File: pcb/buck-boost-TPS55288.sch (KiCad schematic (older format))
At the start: 20 parts

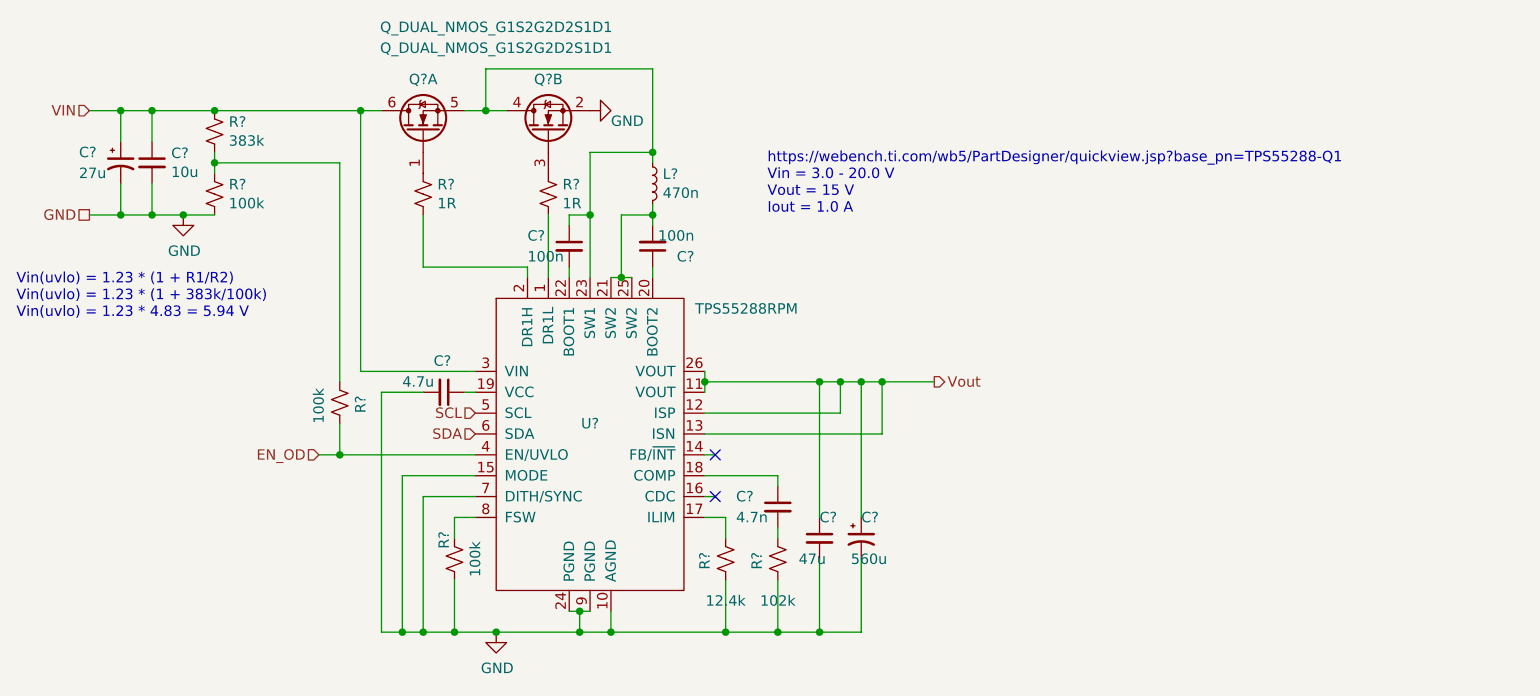
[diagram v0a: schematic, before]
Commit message: [PCB] update mcu config & pwr converter, add sd card
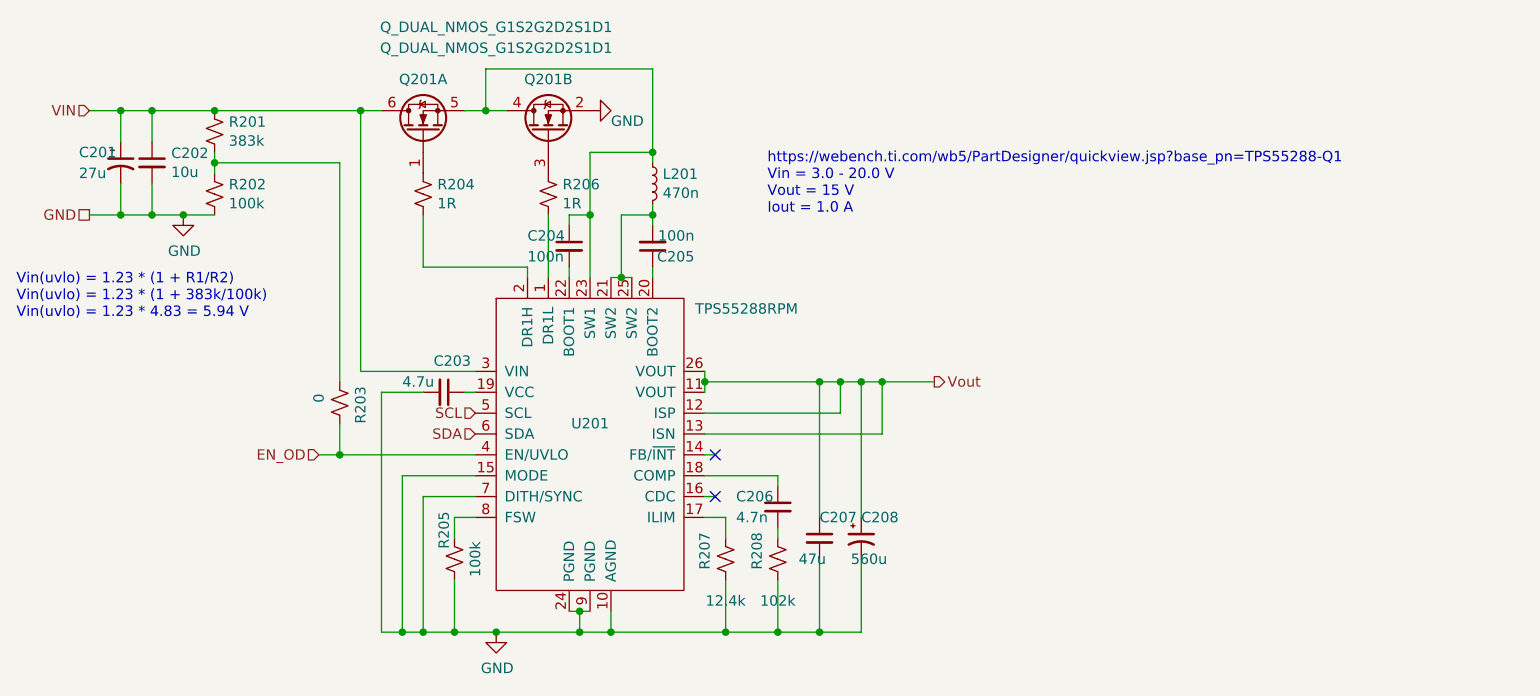
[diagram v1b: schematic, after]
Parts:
- R203: renamed from R?; value 100k -> 0
- gave numbers to parts that had none: 18
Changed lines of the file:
@@
 $Descr A4 11693 8268
 encoding utf-8
-Sheet 2 4
+Sheet 2 5
 Title ""
 Date ""
@@
 $EndDescr
 $Comp
-L project-lib:TPS55288RPM U?
+L project-lib:TPS55288RPM U201
 U 1 1 605DA098
 P 5850 3750
-F 0 "U?" H 5850 3850 50  0000 C CNN
+F 0 "U201" H 5850 3850 50  0000 C CNN
 F 1 "TPS55288RPM" H 6600 4400 50  0000 C CNN
 F 2 "" H 5850 3600 50  0001 C CNN
@@
 GND
 $Comp
-L Device:CP1_Small C?
+L Device:CP1_Small C201
 U 1 1 605DAB16
 P 3600 2400
-F 0 "C?" H 3400 2450 50  0000 L CNN
+F 0 "C201" H 3400 2450 50  0000 L CNN
 F 1 "27u" H 3400 2350 50  0000 L CNN
 F 2 "" H 3600 2400 50  0001 C CNN
@@
 $EndComp
 $Comp
-L Device:R_Small_US R?
+L Device:R_Small_US R201
 U 1 1 605DCCBF
 P 4050 2250
-F 0 "R?" H 4118 2296 50  0000 L CNN
+F 0 "R201" H 4118 2296 50  0000 L CNN
 F 1 "383k" H 4118 2205 50  0000 L CNN
 F 2 "" H 4050 2250 50  0001 C CNN
@@
 $EndComp
 $Comp
-L Device:R_Small_US R?
+L Device:R_Small_US R202
 U 1 1 605DD936
 P 4050 2550
-F 0 "R?" H 4118 2596 50  0000 L CNN
+F 0 "R202" H 4118 2596 50  0000 L CNN
 F 1 "100k" H 4118 2505 50  0000 L CNN
 F 2 "" H 4050 2550 50  0001 C CNN
@@
 Connection ~ 4050 2150
 $Comp
-L Device:R_Small_US R?
+L Device:R_Small_US R204
 U 1 1 605E0D09
 P 5050 2550
-F 0 "R?" H 5118 2596 50  0000 L CNN
+F 0 "R204" H 5118 2596 50  0000 L CNN
 F 1 "1R" H 5118 2505 50  0000 L CNN
 F 2 "" H 5050 2550 50  0001 C CNN
@@
 $EndComp
 $Comp
-L power:GND #PWR?
+L power:GND #PWR0104
 U 1 1 605E1D02
 P 3900 2650
-F 0 "#PWR?" H 3900 2400 50  0001 C CNN
+F 0 "#PWR0104" H 3900 2400 50  0001 C CNN
 F 1 "GND" H 3905 2477 50  0000 C CNN
 F 2 "" H 3900 2650 50  0001 C CNN
@@
 	3900 2650 4050 2650
 $Comp
-L Device:Q_DUAL_NMOS_G1S2G2D2S1D1 Q?
+L Device:Q_DUAL_NMOS_G1S2G2D2S1D1 Q201
 U 1 1 605EB98C
 P 5050 2250
-F 0 "Q?" V 5300 2250 50  0000 C CNN
+F 0 "Q201" V 5300 2250 50  0000 C CNN
 F 1 "Q_DUAL_NMOS_G1S2G2D2S1D1" V 5550 1900 50  0000 C CNN
 F 2 "" H 5250 2250 50  0001 C CNN
@@
 $EndComp
 $Comp
-L Device:Q_DUAL_NMOS_G1S2G2D2S1D1 Q?
+L Device:Q_DUAL_NMOS_G1S2G2D2S1D1 Q201
 U 2 1 605ED468
 P 5650 2250
-F 0 "Q?" V 5900 2250 50  0000 C CNN
+F 0 "Q201" V 5900 2250 50  0000 C CNN
 F 1 "Q_DUAL_NMOS_G1S2G2D2S1D1" V 6050 2500 50  0000 C CNN
 F 2 "" H 5850 2250 50  0001 C CNN
@@
 	5550 2900 5550 2950
 $Comp
-L Device:R_Small_US R?
+L Device:R_Small_US R206
 U 1 1 605F4F86
 P 5650 2550
-F 0 "R?" H 5718 2596 50  0000 L CNN
+F 0 "R206" H 5718 2596 50  0000 L CNN
 F 1 "1R" H 5718 2505 50  0000 L CNN
 F 2 "" H 5650 2550 50  0001 C CNN
@@
 	5650 2650 5650 2950
 $Comp
-L power:GND #PWR?
+L power:GND #PWR0105
 U 1 1 605F59CE
 P 5850 2150
-F 0 "#PWR?" H 5850 1900 50  0001 C CNN
+F 0 "#PWR0105" H 5850 1900 50  0001 C CNN
 F 1 "GND" V 5800 2050 50  0000 R CNN
 F 2 "" H 5850 2150 50  0001 C CNN
@@
 $EndComp
 $Comp
-L Device:C_Small C?
+L Device:C_Small C202
 U 1 1 605F65FF
 P 3750 2400
-F 0 "C?" H 3842 2446 50  0000 L CNN
+F 0 "C202" H 3842 2446 50  0000 L CNN
 F 1 "10u" H 3842 2355 50  0000 L CNN
 F 2 "" H 3750 2400 50  0001 C CNN
@@
 $EndComp
 $Comp
-L Device:C_Small C?
+L Device:C_Small C204
 U 1 1 605F7034
 P 5750 2800
-F 0 "C?" H 5550 2850 50  0000 L CNN
+F 0 "C204" H 5550 2850 50  0000 L CNN
 F 1 "100n" H 5550 2750 50  0000 L CNN
 F 2 "" H 5750 2800 50  0001 C CNN
@@
 	5850 2650 5850 2950
 $Comp
-L Device:L_Small L?
+L Device:L_Small L201
 U 1 1 605FE001
 P 6150 2500
-F 0 "L?" H 6198 2546 50  0000 L CNN
+F 0 "L201" H 6198 2546 50  0000 L CNN
 F 1 "470n" H 6198 2455 50  0000 L CNN
 F 2 "" H 6150 2500 50  0001 C CNN
@@
 Connection ~ 5850 2650
 $Comp
-L Device:C_Small C?
+L Device:C_Small C205
 U 1 1 605FFF8F
 P 6150 2800
-F 0 "C?" H 5950 2850 50  0000 L CNN
+F 0 "C205" H 5950 2850 50  0000 L CNN
 F 1 "100n" H 5950 2750 50  0000 L CNN
 F 2 "" H 6150 2800 50  0001 C CNN
@@
 	6400 3450 6400 3500
 $Comp
-L Device:CP1_Small C?
+L Device:CP1_Small C208
 U 1 1 606075B0
 P 7150 4200
-F 0 "C?" H 7150 4300 50  0000 L CNN
+F 0 "C208" H 7150 4300 50  0000 L CNN
 F 1 "560u" H 7100 4100 50  0000 L CNN
 F 2 "" H 7150 4200 50  0001 C CNN
@@
 	7150 4100 7150 3450
 $Comp
-L Device:C_Small C?
+L Device:C_Small C207
 U 1 1 606075B8
 P 6950 4200
-F 0 "C?" H 6950 4300 50  0000 L CNN
+F 0 "C207" H 6950 4300 50  0000 L CNN
 F 1 "47u" H 6850 4100 50  0000 L CNN
 F 2 "" H 6950 4200 50  0001 C CNN
@@
 	6400 3800 6450 3800
 $Comp
-L Device:C_Small C?
+L Device:C_Small C206
 U 1 1 6061585F
 P 6750 4050
-F 0 "C?" H 6550 4100 50  0000 L CNN
+F 0 "C206" H 6550 4100 50  0000 L CNN
 F 1 "4.7n" H 6550 4000 50  0000 L CNN
 F 2 "" H 6750 4050 50  0001 C CNN
@@
 $EndComp
 $Comp
-L Device:R_Small_US R?
+L Device:R_Small_US R208
 U 1 1 60616C76
 P 6750 4300
-F 0 "R?" V 6850 4350 50  0000 R CNN
+F 0 "R208" V 6850 4350 50  0000 R CNN
 F 1 "102k" H 6750 4500 50  0000 C CNN
 F 2 "" H 6750 4300 50  0001 C CNN
@@
 	6400 4000 6450 4000
 $Comp
-L Device:R_Small_US R?
+L Device:R_Small_US R207
 U 1 1 60620225
 P 6500 4300
-F 0 "R?" V 6600 4350 50  0000 R CNN
+F 0 "R207" V 6600 4350 50  0000 R CNN
 F 1 "12.4k" H 6500 4500 50  0000 C CNN
 F 2 "" H 6500 4300 50  0001 C CNN
@@
 	6500 4400 6500 4650
 $Comp
-L Device:C_Small C?
+L Device:C_Small C203
 U 1 1 60622B20
 P 5150 3500
-F 0 "C?" V 5000 3450 50  0000 L CNN
+F 0 "C203" V 5000 3450 50  0000 L CNN
 F 1 "4.7u" V 5100 3300 50  0000 L CNN
 F 2 "" H 5150 3500 50  0001 C CNN
@@
 	5250 3500 5300 3500
 $Comp
-L Device:R_Small_US R?
+L Device:R_Small_US R205
 U 1 1 606282CE
 P 5200 4300
-F 0 "R?" V 5250 4250 50  0000 R CNN
+F 0 "R205" V 5250 4250 50  0000 R CNN
 F 1 "100k" V 5100 4300 50  0000 C CNN
 F 2 "" H 5200 4300 50  0001 C CNN
@@
 Connection ~ 4950 4650
 $Comp
-L power:GND #PWR?
+L power:GND #PWR0106
 U 1 1 6063E10D
 P 5400 4650
-F 0 "#PWR?" H 5400 4400 50  0001 C CNN
+F 0 "#PWR0106" H 5400 4400 50  0001 C CNN
 F 1 "GND" H 5405 4477 50  0000 C CNN
 F 2 "" H 5400 4650 50  0001 C CNN
@@
 Text HLabel 4550 3800 0    50   Input ~ 0
 EN_OD
-$Comp
-L Device:R_Small_US R?
+Wire Wire Line
+	4650 3450 4650 2400
+Wire Wire Line
+	4650 3650 4650 3800
+Connection ~ 4650 3800
+Wire Wire Line
+	4650 3800 5300 3800
+Text Notes 3100 3150 0    50   ~ 0
+Vin(uvlo) = 1.23 * (1 + R1/R2)\nVin(uvlo) = 1.23 * (1 + 383k/100k)\nVin(uvlo) = 1.23 * 4.83 = 5.94 V
+$Comp
+L Device:R_Small_US R203
 U 1 1 60640262
 P 4650 3550
-F 0 "R?" V 4750 3500 50  0000 L CNN
-F 1 "100k" V 4550 3450 50  0000 L CNN
+F 0 "R203" V 4750 3450 50  0000 L CNN
+F 1 "0" V 4550 3550 50  0000 L CNN
 F 2 "" H 4650 3550 50  0001 C CNN
 F 3 "~" H 4650 3550 50  0001 C CNN
@@
 	1    0    0    -1
 $EndComp
-Wire Wire Line
-	4650 3450 4650 2400
-Wire Wire Line
-	4650 3650 4650 3800
-Connection ~ 4650 3800
-Wire Wire Line
-	4650 3800 5300 3800
-Text Notes 3100 3150 0    50   ~ 0
-Vin(uvlo) = 1.23 * (1 + R1/R2)\nVin(uvlo) = 1.23 * (1 + 383k/100k)\nVin(uvlo) = 1.23 * 4.83 = 5.94 V
 $EndSCHEMATC

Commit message: [PCB] minor changes
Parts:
- removed C203: 4.7u, symbol Device:C_Small
- removed C204, C205: 100n, symbol Device:C_Small
- removed C206: 4.7n, symbol Device:C_Small
- removed C207: 47u, symbol Device:C_Small
- removed C208: 560u, symbol Device:CP1_Small
- removed L201: 470n, symbol Device:L_Small
- removed R201: 383k, symbol Device:R_Small_US
- removed R202, R205: 100k, symbol Device:R_Small_US
- removed R203: 0, symbol Device:R_Small_US
- removed R204, R206: 1R, symbol Device:R_Small_US
- removed R207: 12.4k, symbol Device:R_Small_US
- removed R208: 102k, symbol Device:R_Small_US
- added C?: 4.7u, Capacitor_SMD:C_0603_1608Metric, symbol Device:C_Small
- added C?: 4.7n, Capacitor_SMD:C_0603_1608Metric, symbol Device:C_Small
- added C?: 47u, Capacitor_SMD:C_0603_1608Metric, symbol Device:C_Small
- added C?: 560u, Capacitor_SMD:C_0603_1608Metric, symbol Device:CP1_Small
- added C? (x2): 100n, Capacitor_SMD:C_0603_1608Metric, symbol Device:C_Small
- added L?: 470n, symbol Device:L_Small
- added R?: 383k, symbol Device:R_Small
- added R? (x2): 100k, symbol Device:R_Small
- added R? (x2): 1R, symbol Device:R_Small
- added R?: 0, symbol Device:R_Small
- added R?: 12.4k, symbol Device:R_Small
- added R?: 102k, symbol Device:R_Small
- C201, C202: footprint (none) -> Capacitor_SMD:C_0603_1608Metric
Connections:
- net GND: now also C?.2, C?.2, C?.2, R?.1, R?.1, R?.2, R?.2
- net VIN: now also R?.2
- net Vout: now also C?.1, C?.1
- net at U201.1 (DR1L): now also R?.1
- net at U201.17 (ILIM): now also R?.1
- net at U201.18 (COMP): now also C?.1
- net at U201.19 (VCC): now also C?.1
- net at U201.2 (DR1H): now also R?.1
- net at U201.20 (BOOT2): now also C?.2
- net at U201.21 (SW2), U201.25 (SW2): now also C?.1, L?.2
- net at U201.22 (BOOT1): now also C?.2
- net at Q201.4 (D), Q201.5 (S), U201.23 (SW1): now also C?.1, L?.1
- net at U201.8 (FSW): now also R?.2
- net at Q201.1 (G): now also R?.2
- net at Q201.3 (G): now also R?.2
- net EN_OD renamed ~EN_OD
- net ~EN_OD: now also R?.1
- new net: R?.1, R?.2, R?.2
- new net: C?.2, R?.1
